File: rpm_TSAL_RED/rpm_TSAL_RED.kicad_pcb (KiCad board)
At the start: 2 copper layers, 50.1 x 50.8 mm, 37 parts, among them Q1 NMOS, Q2 PMOS, U1 NE555D, U2 TBA1-0511E, U3 SFH617A-1X007T, U4 OPA355NA

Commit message: Added Sub project
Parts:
- added J1: Conn_01x04, wuerth_conn:66200411022, F.Cu at (124.0, 91.4)
- added J3: Conn_01x02, wuerth_conn:657002130101, F.Cu at (156.1, 115.4)
- moved R13 64.0 mm to (168.3, 92.9)
- moved R14 62.7 mm to (164.6, 96.9), turned to -90 degrees
- moved H3 62.5 mm to (142.7, 96.4)
- moved R12 62.1 mm to (169.1, 86.9), turned to 90 degrees
- moved R15 60.6 mm to (160.1, 100.2), turned to 180 degrees
- moved R11 59.4 mm to (168.3, 81.1), turned to 180 degrees
- moved R16 59.0 mm to (156.1, 103.5), turned to 90 degrees
- moved R8 57.3 mm to (160.0, 77.4), turned to 180 degrees
- moved C6 57.2 mm to (163.2, 72.1)
- moved R4 57.2 mm to (138.0, 82.9)
- moved R17 56.4 mm to (142.8, 87.2), turned to 180 degrees
- moved C7 56.3 mm to (163.2, 73.6)
- moved H2 56.3 mm to (129.0, 87.5)
- moved R10 55.9 mm to (167.4, 77.8), turned to -90 degrees
- moved R5 55.7 mm to (141.4, 83.8)
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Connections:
- net /TS- renamed HV_RED-
- R16 pad 1: /TS+ -> HV_RED+
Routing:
- net (no net): track 269.3 -> 0.00 mm, vias 13 -> 0
- net HV_RED-: track 0.00 -> 79.9 mm, vias 0 -> 2
- net +5V: track 0.00 -> 49.8 mm, vias 0 -> 2
- net +5V_{iso_RED}: track 0.00 -> 19.9 mm
- net +24V: track 0.00 -> 17.1 mm
- net GND: track 0.00 -> 13.0 mm, vias 0 -> 7
- net /TSAL_RED_LED_SW: track 0.00 -> 12.3 mm
- net Net-(U1-R): track 0.00 -> 9.93 mm
- net Net-(U1-THR): track 0.00 -> 9.75 mm
- net Net-(U4-+): track 0.00 -> 9.50 mm
- net Net-(Q1-G): track 0.00 -> 8.52 mm
- net HV_RED+: track 0.00 -> 5.28 mm
- net Net-(R12-Pad1): track 0.00 -> 5.13 mm
- net Net-(U3-Pad1): track 0.00 -> 4.95 mm
- net Net-(R11-Pad1): track 0.00 -> 4.95 mm
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- added copper zone on B.Cu, net GND
- removed copper zone on B.Cu, net (none)
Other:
- outline, holes or cut-outs redrawn
- copper layers 2 -> 4

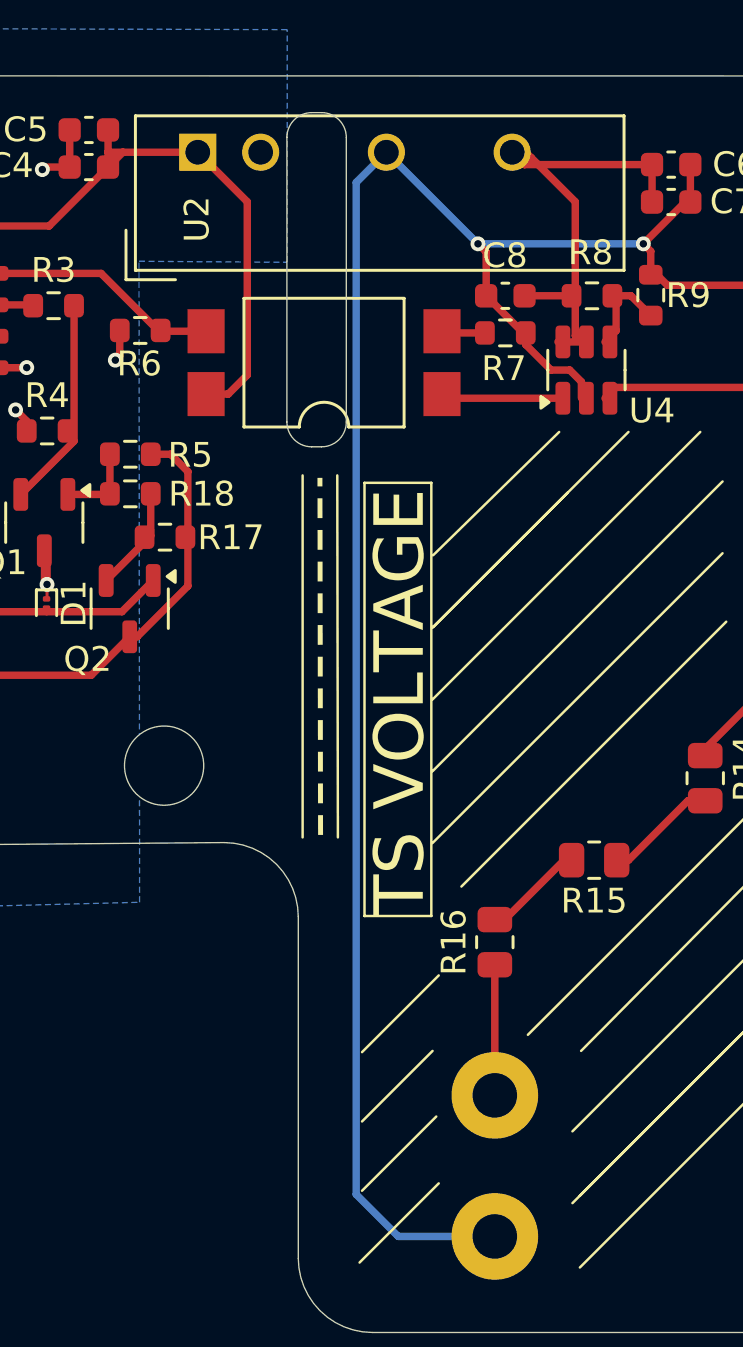
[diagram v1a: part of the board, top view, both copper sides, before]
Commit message: Added TSAC Indicator with PSU
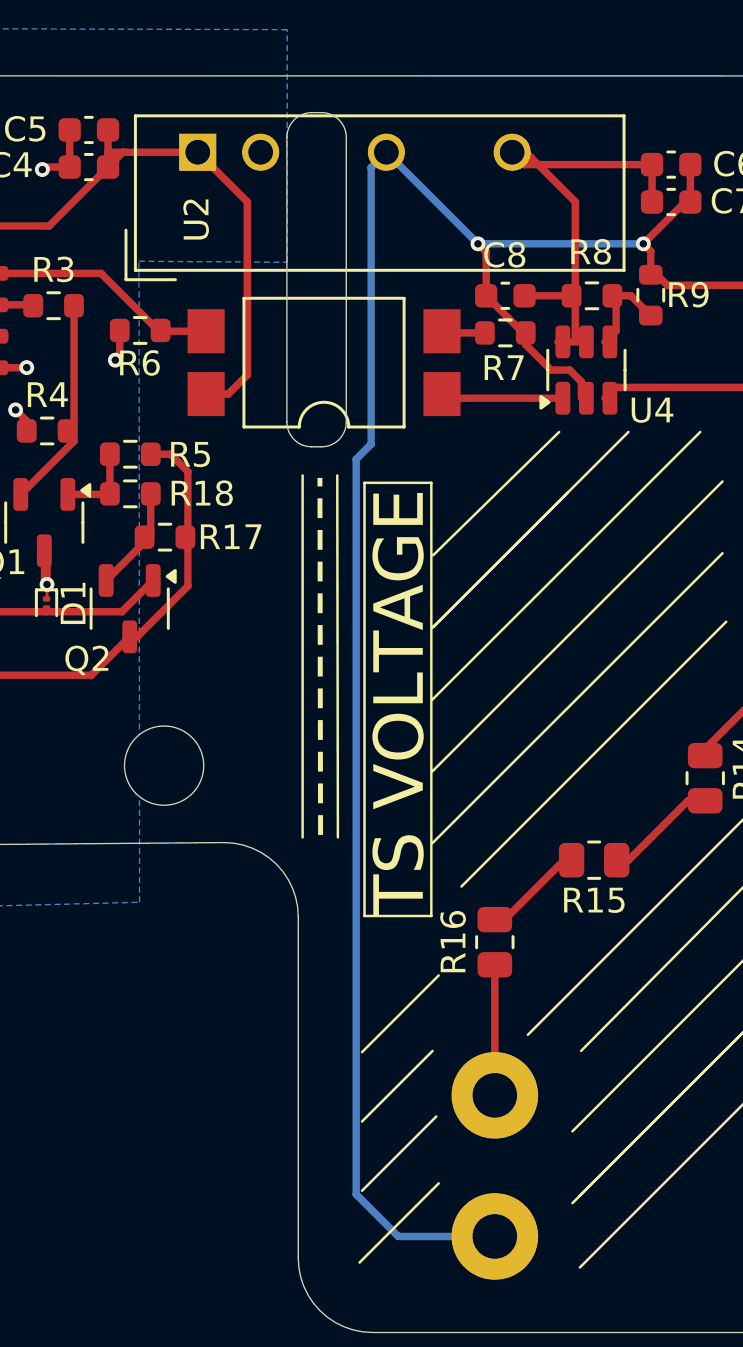
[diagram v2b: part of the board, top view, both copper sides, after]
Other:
- copper layers 4 -> 2
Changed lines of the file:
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@@
 	(layers
 		(0 "F.Cu" signal)
-		(1 "In1.Cu" signal)
-		(2 "In2.Cu" signal)
 		(31 "B.Cu" signal)
 		(32 "B.Adhes" user "B.Adhesive")
@@
 			)
 			(layer "dielectric 1"
-				(type "prepreg")
-				(color "FR4 natural")
-				(thickness 0.138)
-				(material "Pansonic R-1551(W)")
-				(epsilon_r 4.3)
-				(loss_tangent 0)
-			)
-			(layer "In1.Cu"
-				(type "copper")
-				(thickness 0.035)
-			)
-			(layer "dielectric 2"
 				(type "core")
 				(color "FR4 natural")
-				(thickness 1.113)
-				(material "Panasonic R-1566(W)")
-				(epsilon_r 4.6)
-				(loss_tangent 0)
-			)
-			(layer "In2.Cu"
-				(type "copper")
-				(thickness 0.035)
-			)
-			(layer "dielectric 3"
-				(type "prepreg")
-				(color "FR4 natural")
-				(thickness 0.138)
+				(thickness 1.459)
 				(material "Pansonic R-1551(W)")
 				(epsilon_r 4.3)
@@
 	)
 	(segment
-		(start 152.2 115.4)
-		(end 150.5 113.7)
+		(start 162.1 75.3)
+		(end 155.42 75.3)
 		(width 0.3)
 		(layer "B.Cu")
@@
 	)
 	(segment
-		(start 162.1 75.3)
-		(end 155.42 75.3)
+		(start 150.5 113.7)
+		(end 150.5 84)
 		(width 0.3)
 		(layer "B.Cu")
@@
 	)
 	(segment
-		(start 150.5 72.82)
-		(end 151.72 71.6)
+		(start 151.1 83.4)
+		(end 151.1 72.22)
 		(width 0.3)
 		(layer "B.Cu")
@@
 	)
 	(segment
-		(start 155.42 75.3)
+		(start 151.1 72.22)
 		(end 151.72 71.6)
 		(width 0.3)
@@
 	)
 	(segment
-		(start 150.5 113.7)
-		(end 150.5 72.82)
+		(start 150.5 84)
+		(end 151.1 83.4)
+		(width 0.3)
+		(layer "B.Cu")
+		(net 23)
+	)
+	(segment
+		(start 152.2 115.4)
+		(end 150.5 113.7)
+		(width 0.3)
+		(layer "B.Cu")
+		(net 23)
+	)
+	(segment
+		(start 155.42 75.3)
+		(end 151.72 71.6)
 		(width 0.3)
 		(layer "B.Cu")
